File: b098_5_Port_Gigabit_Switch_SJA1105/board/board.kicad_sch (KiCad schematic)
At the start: 7 parts, among them J1 DebugEdge_02x05, J2 002_SPI

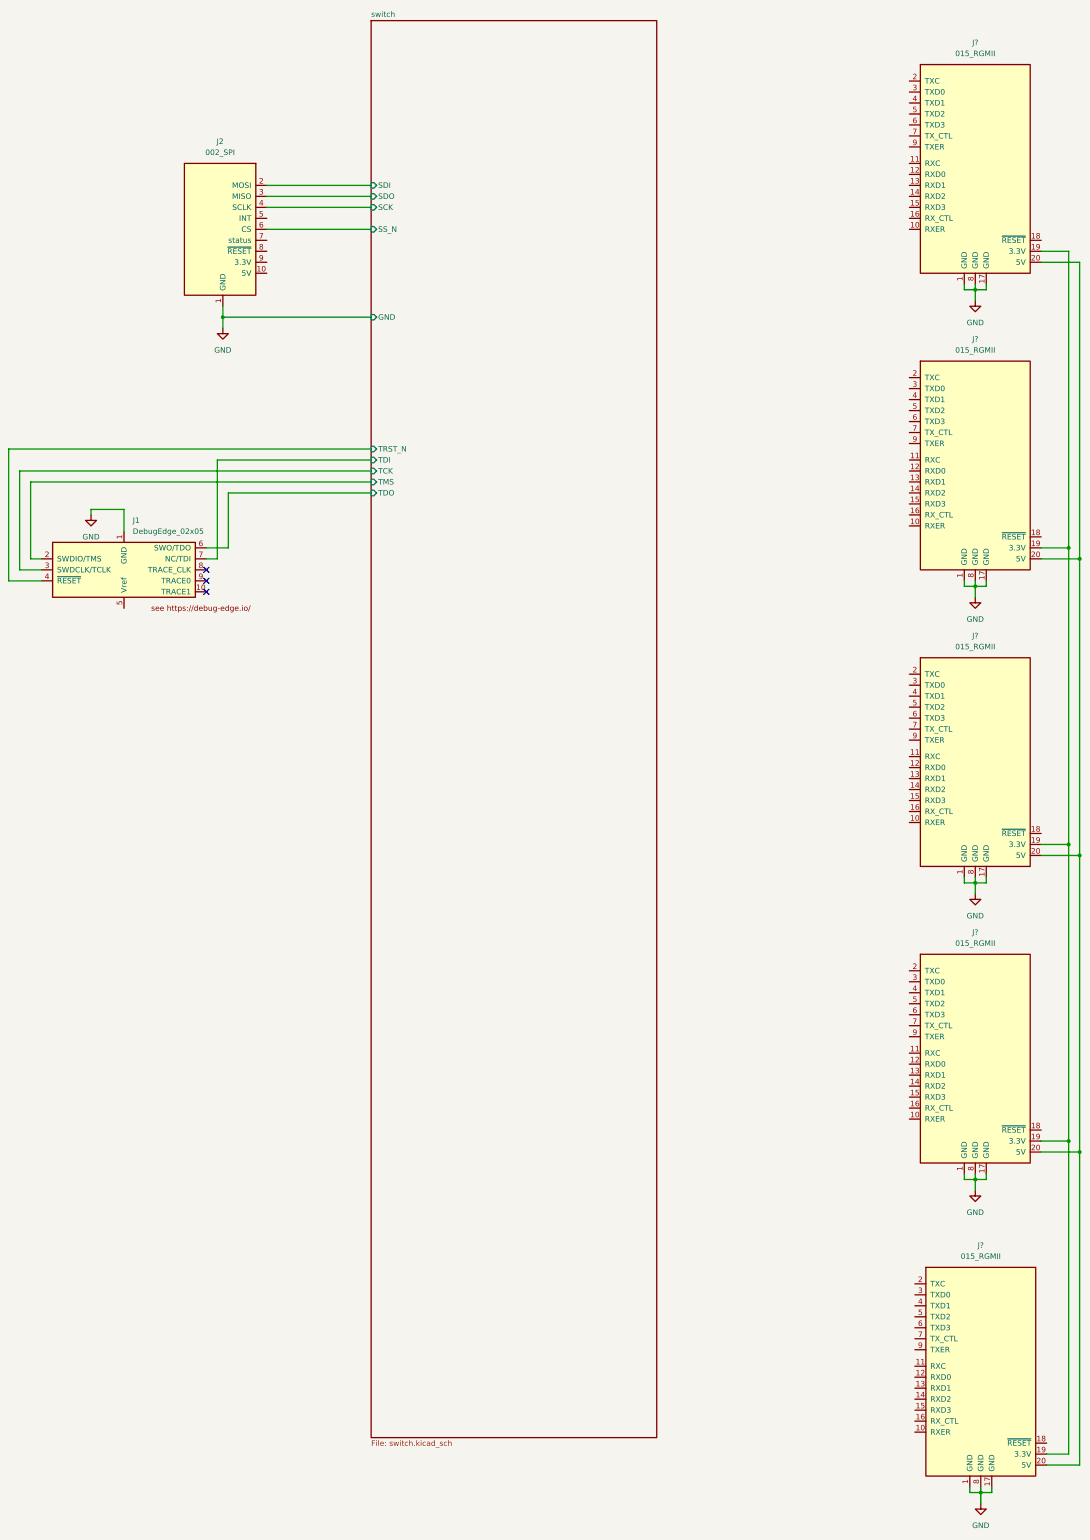
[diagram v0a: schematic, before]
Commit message: added the rest of the MII interfaces
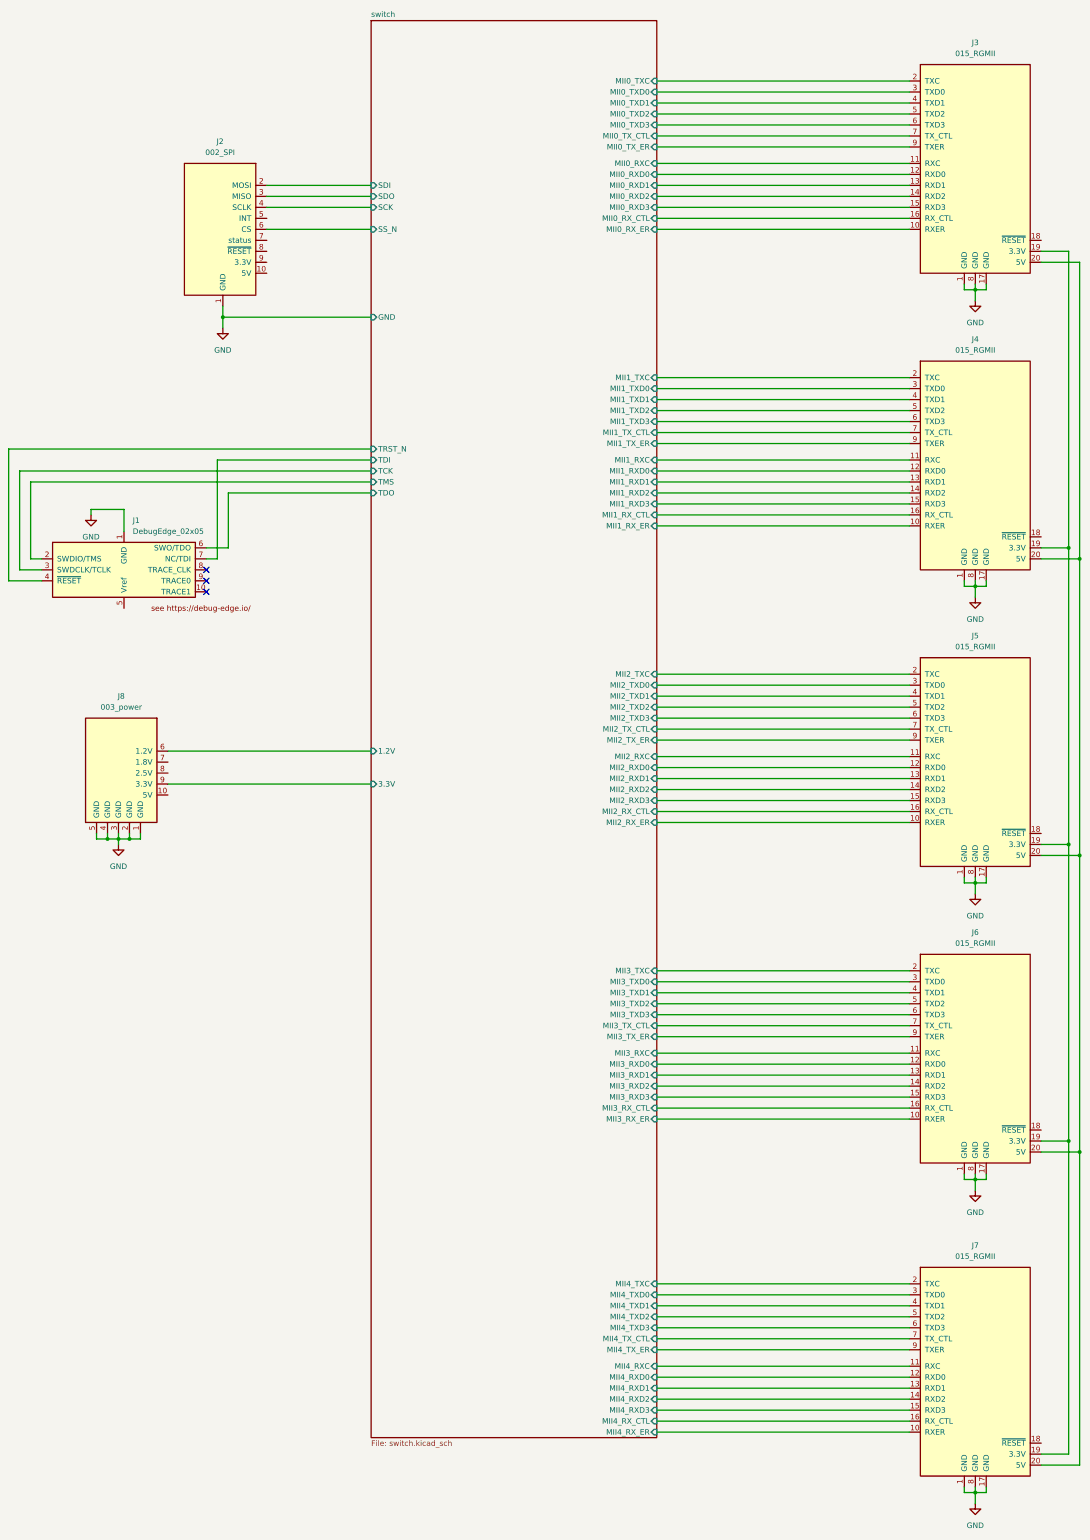
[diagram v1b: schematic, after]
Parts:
- added J8: 003_power, on_edge:on_edge_2x05_device, symbol put_on_edge:003_power
- J3, J4, J5, J6, J7: renamed from J?; footprint (none) -> on_edge:on_edge_2x10_host
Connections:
- net GND: now also J8.1 (GND), J8.2 (GND), J8.3 (GND), J8.4 (GND), J8.5 (GND)
- net switch/MII2_RX_ER: now reaches J5.10 (RXER)
- net switch/MII2_RXC: now reaches J5.11 (RXC)
- net switch/MII2_RXD0: now reaches J5.12 (RXD0)
- net switch/MII2_RXD1: now reaches J5.13 (RXD1)
- net switch/MII2_RXD2: now reaches J5.14 (RXD2)
- net switch/MII2_RXD3: now reaches J5.15 (RXD3)
- net switch/MII2_RX_CTL: now reaches J5.16 (RX_CTL)
- net switch/MII2_TXC: now reaches J5.2 (TXC)
- net switch/MII2_TXD0: now reaches J5.3 (TXD0)
- net switch/MII2_TXD1: now reaches J5.4 (TXD1)
- net switch/MII2_TXD2: now reaches J5.5 (TXD2)
- net switch/MII2_TXD3: now reaches J5.6 (TXD3)
- net switch/MII2_TX_CTL: now reaches J5.7 (TX_CTL)
- net switch/MII2_TX_ER: now reaches J5.9 (TXER)
- net switch/MII0_RX_ER: now reaches J3.10 (RXER)
- net switch/MII0_RXC: now reaches J3.11 (RXC)
- net switch/MII0_RXD0: now reaches J3.12 (RXD0)
- net switch/MII0_RXD1: now reaches J3.13 (RXD1)
- net switch/MII0_RXD2: now reaches J3.14 (RXD2)
- net switch/MII0_RXD3: now reaches J3.15 (RXD3)
- net switch/MII0_RX_CTL: now reaches J3.16 (RX_CTL)
- net switch/MII0_TXC: now reaches J3.2 (TXC)
- net switch/MII0_TXD0: now reaches J3.3 (TXD0)
- net switch/MII0_TXD1: now reaches J3.4 (TXD1)
- net switch/MII0_TXD2: now reaches J3.5 (TXD2)
- net switch/MII0_TXD3: now reaches J3.6 (TXD3)
- net switch/MII0_TX_CTL: now reaches J3.7 (TX_CTL)
- net switch/MII0_TX_ER: now reaches J3.9 (TXER)
- net switch/MII1_RX_ER: now reaches J4.10 (RXER)
- net switch/MII1_RXC: now reaches J4.11 (RXC)
- net switch/MII1_RXD0: now reaches J4.12 (RXD0)
- net switch/MII1_RXD1: now reaches J4.13 (RXD1)
- net switch/MII1_RXD2: now reaches J4.14 (RXD2)
- net switch/MII1_RXD3: now reaches J4.15 (RXD3)
- net switch/MII1_RX_CTL: now reaches J4.16 (RX_CTL)
- net switch/MII1_TXC: now reaches J4.2 (TXC)
- net switch/MII1_TXD0: now reaches J4.3 (TXD0)
- net switch/MII1_TXD1: now reaches J4.4 (TXD1)
- net switch/MII1_TXD2: now reaches J4.5 (TXD2)
- net switch/MII1_TXD3: now reaches J4.6 (TXD3)
- net switch/MII1_TX_CTL: now reaches J4.7 (TX_CTL)
- net switch/MII1_TX_ER: now reaches J4.9 (TXER)
- net switch/MII4_RX_ER: now reaches J7.10 (RXER)
- net switch/MII4_RXC: now reaches J7.11 (RXC)
- net switch/MII4_RXD0: now reaches J7.12 (RXD0)
- net switch/MII4_RXD1: now reaches J7.13 (RXD1)
- net switch/MII4_RXD2: now reaches J7.14 (RXD2)
- net switch/MII4_RXD3: now reaches J7.15 (RXD3)
- net switch/MII4_RX_CTL: now reaches J7.16 (RX_CTL)
- net switch/MII4_TXC: now reaches J7.2 (TXC)
- net switch/MII4_TXD0: now reaches J7.3 (TXD0)
- net switch/MII4_TXD1: now reaches J7.4 (TXD1)
- net switch/MII4_TXD2: now reaches J7.5 (TXD2)
- net switch/MII4_TXD3: now reaches J7.6 (TXD3)
- net switch/MII4_TX_CTL: now reaches J7.7 (TX_CTL)
- net switch/MII4_TX_ER: now reaches J7.9 (TXER)
- net switch/MII3_RX_ER: now reaches J6.10 (RXER)
- net switch/MII3_RXC: now reaches J6.11 (RXC)
- net switch/MII3_RXD0: now reaches J6.12 (RXD0)
- net switch/MII3_RXD1: now reaches J6.13 (RXD1)
- net switch/MII3_RXD2: now reaches J6.14 (RXD2)
- net switch/MII3_RXD3: now reaches J6.15 (RXD3)
- net switch/MII3_RX_CTL: now reaches J6.16 (RX_CTL)
- net switch/MII3_TXC: now reaches J6.2 (TXC)
- net switch/MII3_TXD0: now reaches J6.3 (TXD0)
- net switch/MII3_TXD1: now reaches J6.4 (TXD1)
- net switch/MII3_TXD2: now reaches J6.5 (TXD2)
- net switch/MII3_TXD3: now reaches J6.6 (TXD3)
- net switch/MII3_TX_CTL: now reaches J6.7 (TX_CTL)
- net switch/MII3_TX_ER: now reaches J6.9 (TXER)
- new net switch/1.2V: J8.6 (1.2V)
- new net switch/3.3V: J8.9 (3.3V)
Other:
- sheet switch ports: added 1.2V, 3.3V, MII0_RXC, MII0_RXD0, MII0_RXD1, MII0_RXD2, MII0_RXD3, MII0_RX_CTL, MII0_RX_ER, MII0_TXC, MII0_TXD0, MII0_TXD1, MII0_TXD2, MII0_TXD3, MII0_TX_CTL, MII0_TX_ER, MII1_RXC, MII1_RXD0, MII1_RXD1, MII1_RXD2, MII1_RXD3, MII1_RX_CTL, MII1_RX_ER, MII1_TXC, MII1_TXD0, MII1_TXD1, MII1_TXD2, MII1_TXD3, MII1_TX_CTL, MII1_TX_ER, MII2_RXC, MII2_RXD0, MII2_RXD1, MII2_RXD2, MII2_RXD3, MII2_RX_CTL, MII2_RX_ER, MII2_TXC, MII2_TXD0, MII2_TXD1, MII2_TXD2, MII2_TXD3, MII2_TX_CTL, MII2_TX_ER, MII3_RXC, MII3_RXD0, MII3_RXD1, MII3_RXD2, MII3_RXD3, MII3_RX_CTL, MII3_RX_ER, MII3_TXC, MII3_TXD0, MII3_TXD1, MII3_TXD2, MII3_TXD3, MII3_TX_CTL, MII3_TX_ER, MII4_RXC, MII4_RXD0, MII4_RXD1, MII4_RXD2, MII4_RXD3, MII4_RX_CTL, MII4_RX_ER, MII4_TXC, MII4_TXD0, MII4_TXD1, MII4_TXD2, MII4_TXD3, MII4_TX_CTL, MII4_TX_ER; removed none
- moved on the sheet: J7
